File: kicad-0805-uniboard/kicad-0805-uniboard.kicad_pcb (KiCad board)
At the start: 2 copper layers, 100 x 110 mm, 140 parts, among them J1 ICSP Header, J102 Conn_01x16_Male, J103 BA56_3DIG_7SEG, J104 Gate Out, J105 Clock Out, J106 Clock In, J107 Pitch Out, J108 CV Out, J109 Reset In, J4 RED_STRIPE, Q1 2N7002, Q101 MMBT3906, Q102 MMBT3906, Q103 MMBT3906, Q104 MMBT3904, Q105 MMBT3904, Q2 2N7002, Q3 2N7002, Q4 2N7002, SW101 Shift, SW102 Play, SW103 Load, SW104 Save, SW105 Repeat, SW106 Mutate, SW107 Glide, SW108 SW_Push, SW109 SW_Push, SW110 SW_Push, SW111 SW_Push, SW112 SW_Push, SW113 SW_Push, SW114 SW_Push, SW115 SW_Push, SW116 Rotary_Encoder, SW117 SW_Push, SW118 SW_Push, SW119 SW_Push, SW120 SW_Push, SW121 SW_Push, SW122 SW_Push, SW123 SW_Push, SW124 SW_Push, U1 AMS1117-5.0, U101 74HC595, U102 MCP23S17, U103 74HC595, U2 AMS1117-3.3, U3 ATMega328P, U4 W25Q80DVSN, U5 TL072, U6 MCP4822, Y1 16 MHz

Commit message: Initial fp's changed. Cleared old routings.
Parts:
- removed J102: Conn_01x16_Male, Pin_Headers:Pin_Header_Straight_1x16_Pitch2.54mm
- added C10: 10uF, Capacitor_SMD:CP_Elec_5x5.7, F.Cu at (220.7, 129.7)
- added C11: 100uF, Capacitor_SMD:CP_Elec_6.3x7.7, F.Cu at (211.0, 130.3)
- added C12: 22uF, Capacitor_SMD:CP_Elec_5x5.7, F.Cu at (219.2, 137.8)
- added C2: 22uF, Capacitor_SMD:CP_Elec_5x5.7, F.Cu at (210.2, 137.8)
- C104, C107: footprint Capacitors_SMD:CP_Elec_6.3x7.7 -> Capacitor_SMD:CP_Elec_5x5.7
- C16: footprint Capacitor_SMD:C_0805_2012Metric_Pad1.15x1.40mm_HandSolder -> Capacitor_SMD:CP_Elec_5x5.7
- RV101, RV102, RV103, RV104: footprint Potentiometers:Potentiometer_Alps_RK09K_Horizontal -> Eurocad:Alpha9mmPot-SemiSMD4
- moved D109 52.6 mm to (130.1, 127.8)
- moved C1 52.6 mm to (240.0, 87.0)
- moved C101 52.6 mm to (131.1, 114.2)
- moved C102 52.6 mm to (126.1, 114.2)
- moved C103 52.6 mm to (123.1, 114.2)
- moved C105 52.6 mm to (66.1, 115.2)
- moved C106 52.6 mm to (68.1, 115.2)
- moved C107 52.6 mm to (148.1, 65.2)
- moved C108 52.6 mm to (139.4, 60.9)
- moved C109 52.6 mm to (139.4, 58.2)
- moved C14 52.6 mm to (215.2, 109.7)
- moved C15 52.6 mm to (226.5, 98.8)
- moved C4 52.6 mm to (241.5, 90.0)
- moved C7 52.6 mm to (210.5, 109.7)
- moved C8 52.6 mm to (240.0, 84.1)
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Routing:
- net +5V: track 413.6 -> 0.00 mm, vias 2 -> 0
- net Net-(SW109-Pad2): track 218.8 -> 0.00 mm
- net Net-(SW108-Pad2): track 146.6 -> 0.00 mm
- net /A3: track 139.7 -> 0.00 mm
- net Net-(D101-Pad1): track 136.6 -> 0.00 mm
- net /A2: track 123.3 -> 0.00 mm
- net ResetIn: track 116.1 -> 0.00 mm
- net Net-(D102-Pad1): track 108.2 -> 0.00 mm
- net Net-(SW112-Pad1): track 107.8 -> 0.00 mm
- net Net-(U101-Pad9): track 100.8 -> 0.00 mm, vias 2 -> 0
- net GND: track 95.8 -> 0.00 mm, vias 14 -> 1
- net Net-(SW117-Pad1): track 94.7 -> 0.00 mm
- net /A1: track 94.4 -> 0.00 mm
- net AD1: track 91.7 -> 0.00 mm
- net Net-(D103-Pad1): track 78.9 -> 0.00 mm
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- added copper zone on F.Cu, net GND
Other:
- outline, holes or cut-outs redrawn

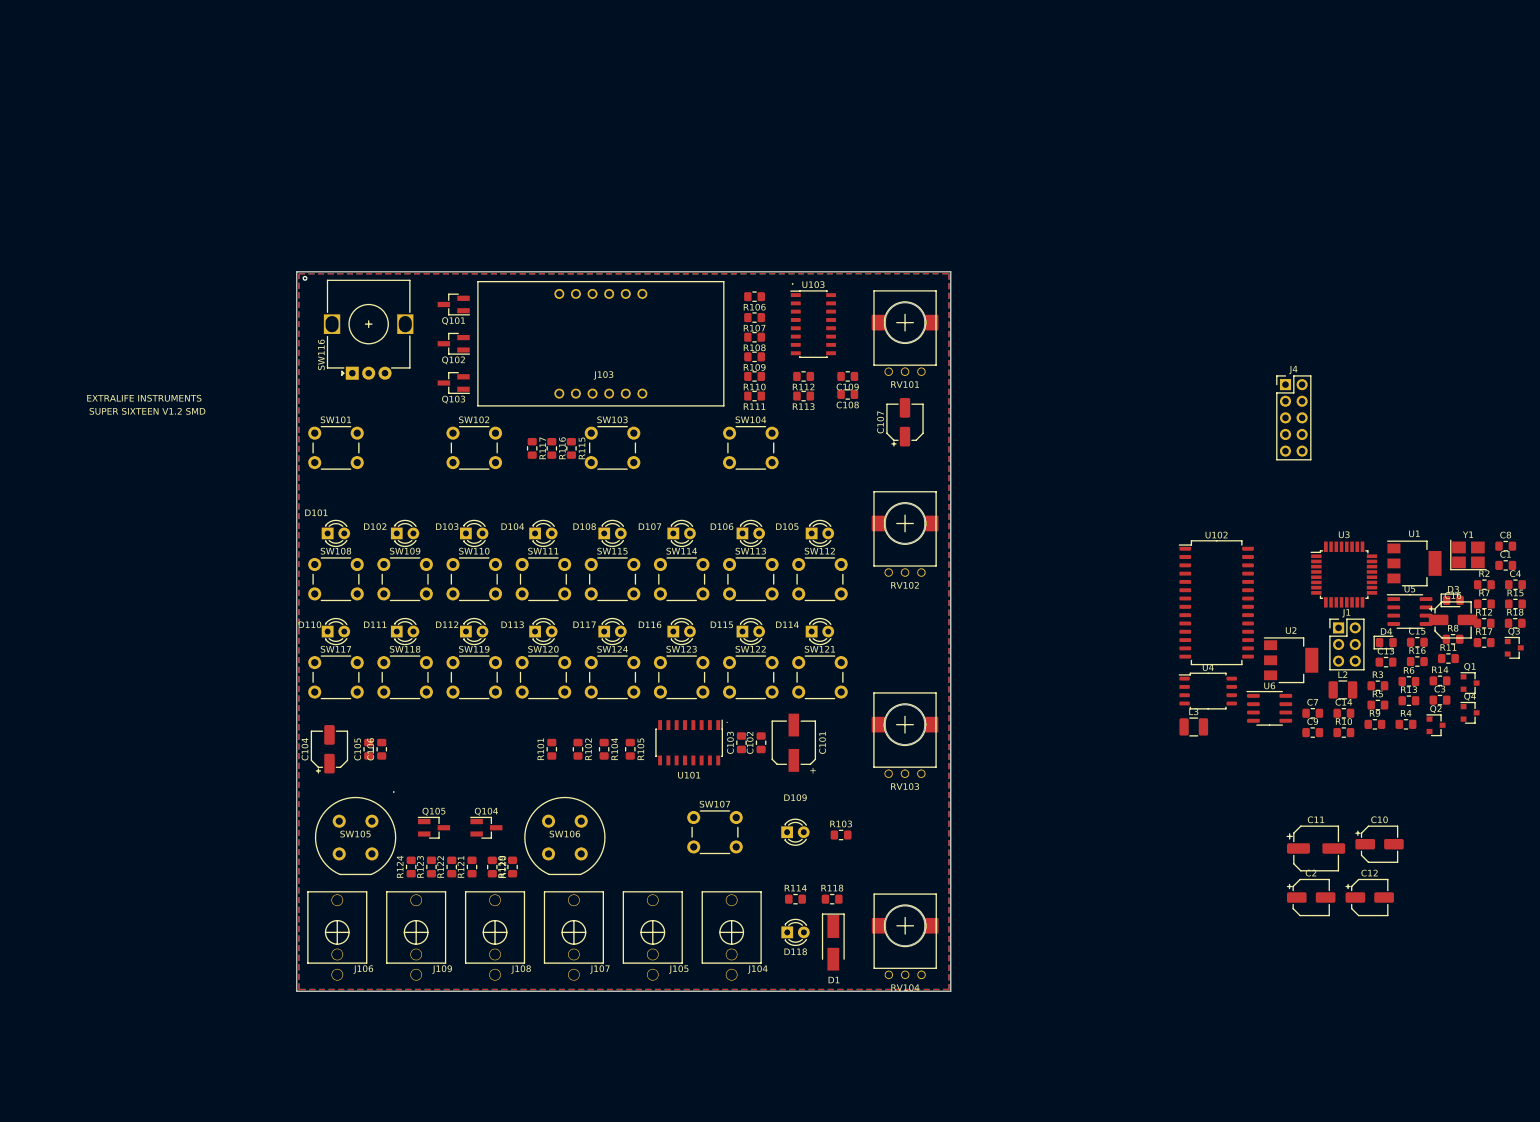
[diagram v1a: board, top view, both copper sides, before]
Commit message: Forgot some schematic stuff. More placement.
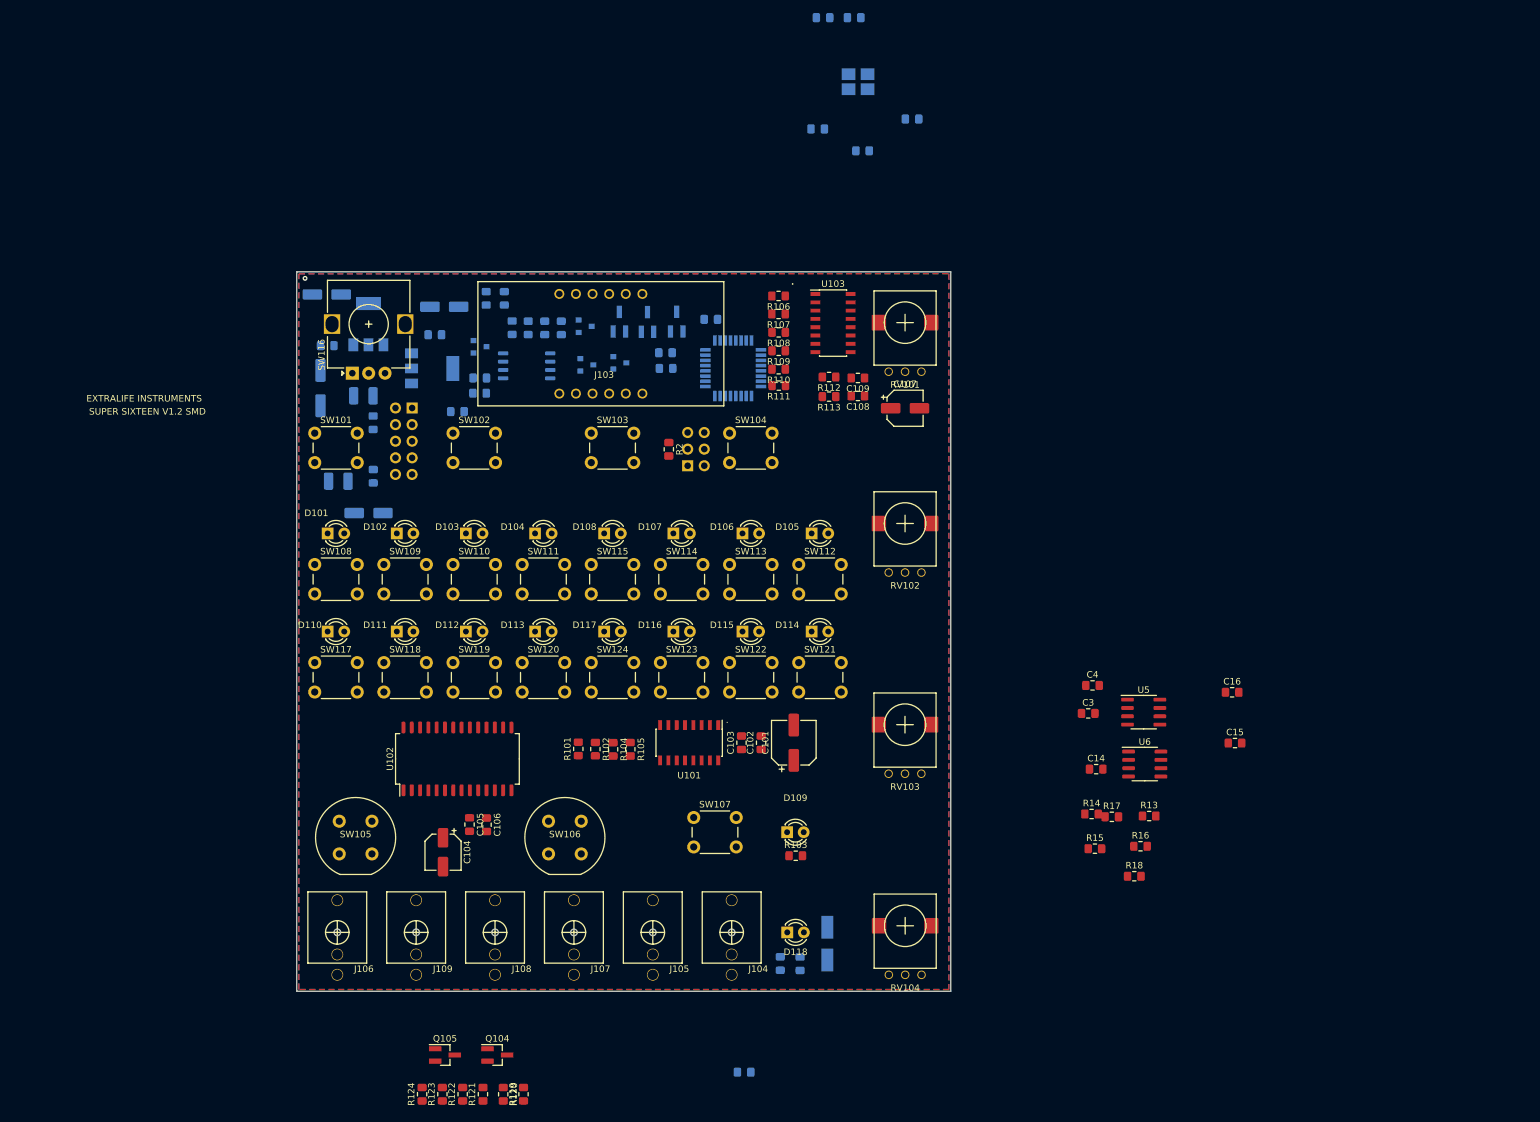
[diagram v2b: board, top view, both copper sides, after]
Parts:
- added C5: 100nF, Capacitor_SMD:C_0805_2012Metric_Pad1.15x1.40mm_HandSolder, B.Cu at (135.6, 3.30)
- added C6: 100nF, Capacitor_SMD:C_0805_2012Metric_Pad1.15x1.40mm_HandSolder, B.Cu at (140.3, 3.30)
- C1, C10, C11, C12, C13, C2, C7, C8, C9, D1, D3, D4, J1, J4, L2, L3, Q1, Q101, Q102, Q103, Q2, Q3, Q4, R10, R11, R114, R115, R116, R117, R118, R12, R3, R4, R5, R6, R7, R8, R9, U1, U2, U3, U4, Y1: moved to B.Cu
- C101: footprint Capacitors_SMD:CP_Elec_6.3x7.7 -> Capacitor_SMD:CP_Elec_6.3x7.7
- C16: footprint Capacitor_SMD:CP_Elec_5x5.7 -> Capacitor_SMD:C_0805_2012Metric_Pad1.15x1.40mm_HandSolder
- moved C1 183.3 mm to (59.8, 53.5)
- moved C2 176.5 mm to (59.7, 45.6)
- moved C11 167.7 mm to (58.8, 59.9), turned to 90 degrees
- moved D3 167.4 mm to (66.8, 65.2), turned to 270 degrees
- moved C10 164.9 mm to (77.7, 47.5), turned to 180 degrees
- moved U1 164.1 mm to (66.1, 50.2), turned to 90 degrees
- moved C12 164.0 mm to (66.1, 79.0), turned to 180 degrees
- moved R7 159.8 mm to (79.7, 63.5), turned to 180 degrees
- moved Q2 157.2 mm to (83.1, 53.6)
- moved D4 157.0 mm to (66.8, 73.4), turned to 270 degrees
- moved L2 156.4 mm to (65.3, 61.1)
- moved R11 153.6 mm to (83.1, 60.7), turned to 180 degrees
- moved R12 153.0 mm to (90.5, 50.7), turned to 270 degrees
- moved C13 148.4 mm to (84.1, 46.2), turned to 270 degrees
- moved Q3 148.2 mm to (99.5, 56.4)
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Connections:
- C11 pad 1: Net-(C11-Pad1) -> +12V
- C12 pad 2: Net-(C12-Pad2) -> -12V
- D3 pad 1: +12V -> Net-(D3-Pad1)
- D4 pad 2: -12V -> Net-(D4-Pad2)
- L2 pad 1: Net-(C11-Pad1) -> +12V
- L2 pad 2: +12V -> Net-(D3-Pad1)
- L3 pad 1: Net-(C12-Pad2) -> -12V
- L3 pad 2: -12V -> Net-(D4-Pad2)
- U3 pad 18: Net-(U3-Pad18) -> +5V
- U3 pad 20: Net-(U3-Pad20) -> +5V
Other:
- outline, holes or cut-outs redrawn

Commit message: More placement work.
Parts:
- C14, C15, C16, C3, C4, Q104, R119, R120, R121, R13, R14, R15, R16, R17, R18, U5, U6: moved to B.Cu
- R4: moved to F.Cu
- moved R119 63.8 mm to (63.9, 109.6), turned to 0 degrees
- moved R122 60.6 mm to (63.9, 109.6), turned to 0 degrees
- moved R120 52.9 mm to (66.2, 119.1)
- moved R121 52.7 mm to (63.6, 119.1), turned to 270 degrees
- moved Q104 52.3 mm to (64.9, 113.9), turned to 270 degrees
- moved R123 50.0 mm to (66.2, 119.1), turned to 270 degrees
- moved R124 49.9 mm to (63.6, 119.1), turned to 270 degrees
- moved Q105 49.7 mm to (64.9, 113.9), turned to 270 degrees
- moved C15 36.4 mm to (162.2, 116.0), turned to 180 degrees
- moved C16 35.6 mm to (162.6, 108.2), turned to 180 degrees
- moved R4 31.9 mm to (110.6, 135.4), turned to 180 degrees
- moved R13 10.3 mm to (175.3, 127.1), turned to 180 degrees
- moved U6 8.98 mm to (176.0, 119.2), turned to 180 degrees
- moved C3 8.66 mm to (184.6, 111.4), turned to 180 degrees
- moved U5 8.66 mm to (176.1, 111.2), turned to 180 degrees
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
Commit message: Prepped to throw more stuff on there..
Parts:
- moved C2 0.35 mm to (59.4, 45.5)
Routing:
- net +5V: track 0.00 -> 89.9 mm
- net +12V: track 0.00 -> 29.7 mm
- net Net-(D3-Pad2): track 0.00 -> 8.33 mm
- net Net-(D3-Pad1): track 0.00 -> 3.09 mm
- net GND: vias 1 -> 0
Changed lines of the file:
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@@
     (thickness 1.6)
     (drawings 16)
-    (tracks 1)
+    (tracks 24)
     (zones 0)
     (modules 145)
@@
   (page A4)
   (layers
-    (0 F.Cu signal)
+    (0 F.Cu signal hide)
     (31 B.Cu signal)
     (32 B.Adhes user)
-    (33 F.Adhes user)
+    (33 F.Adhes user hide)
     (34 B.Paste user)
-    (35 F.Paste user)
+    (35 F.Paste user hide)
     (36 B.SilkS user)
-    (37 F.SilkS user)
+    (37 F.SilkS user hide)
     (38 B.Mask user)
-    (39 F.Mask user)
-    (40 Dwgs.User user)
+    (39 F.Mask user hide)
+    (40 Dwgs.User user hide)
     (41 Cmts.User user)
     (42 Eco1.User user)
@@
     (45 Margin user)
     (46 B.CrtYd user)
-    (47 F.CrtYd user)
+    (47 F.CrtYd user hide)
     (48 B.Fab user)
-    (49 F.Fab user)
+    (49 F.Fab user hide)
   )
   (setup
-    (last_trace_width 0.25)
+    (last_trace_width 0.4)
     (user_trace_width 0.3)
     (user_trace_width 0.35)
@@
   )
   (module Capacitor_SMD:CP_Elec_5x5.7 (layer B.Cu)
-    (at 59.71 45.62)
+    (at 59.39 45.49)
     (descr "SMD capacitor, aluminum electrolytic, United Chemi-Con, 5.0x5.7mm")
     (tags "capacitor electrolytic")
@@
   (gr_line (start 55.12 152.16) (end 155.12 152.16) (layer Edge.Cuts) (width 0.05))
   (gr_line (start 55.12 42.16) (end 55.12 152.16) (layer Edge.Cuts) (width 0.05))
-  (via (at 56.39 43.16) (size 0.75) (drill 0.35) (layers F.Cu B.Cu) (net 1))
+  (segment (start 66.08 51.91) (end 66.08 47.01) (width 0.4) (layer B.Cu) (net 2))
+  (segment (start 66.08 53.31) (end 66.08 51.91) (width 0.4) (layer B.Cu) (net 2))
+  (segment (start 57.51 44.82) (end 59.55 42.78) (width 0.4) (layer B.Cu) (net 2))
+  (segment (start 57.51 45.62) (end 57.51 44.82) (width 0.4) (layer B.Cu) (net 2))
+  (segment (start 59.55 42.78) (end 139.43 42.78) (width 0.4) (layer B.Cu) (net 2))
+  (segment (start 62.305 62.64) (end 63.825 61.12) (width 0.4) (layer B.Cu) (net 83))
+  (segment (start 58.75 62.64) (end 62.305 62.64) (width 0.4) (layer B.Cu) (net 83))
+  (segment (start 60.81 60.58) (end 60.81 53.45) (width 0.4) (layer B.Cu) (net 83))
+  (segment (start 58.75 62.64) (end 60.81 60.58) (width 0.4) (layer B.Cu) (net 83))
+  (segment (start 63.64 53.45) (end 63.78 53.31) (width 0.4) (layer B.Cu) (net 83))
+  (segment (start 60.81 53.45) (end 63.64 53.45) (width 0.4) (layer B.Cu) (net 83))
+  (segment (start 63.78 54.71) (end 64.47 55.4) (width 0.4) (layer B.Cu) (net 83))
+  (segment (start 63.78 53.31) (end 63.78 54.71) (width 0.4) (layer B.Cu) (net 83))
+  (segment (start 64.47 55.4) (end 70.46 55.4) (width 0.4) (layer B.Cu) (net 83))
+  (segment (start 71.23 54.63) (end 72.67 54.63) (width 0.4) (layer B.Cu) (net 83))
+  (segment (start 70.46 55.4) (end 71.23 54.63) (width 0.4) (layer B.Cu) (net 83))
+  (segment (start 72.76 62.98) (end 70.22 62.98) (width 0.4) (layer B.Cu) (net 92))
+  (segment (start 67.5 66.26) (end 68.47 65.29) (width 0.4) (layer B.Cu) (net 92))
+  (segment (start 66.8 66.26) (end 67.5 66.26) (width 0.4) (layer B.Cu) (net 92))
+  (segment (start 68.47 65.29) (end 68.47 63.56) (width 0.4) (layer B.Cu) (net 92))
+  (segment (start 68.47 63.56) (end 69.03 63) (width 0.4) (layer B.Cu) (net 92))
+  (segment (start 70.2 63) (end 70.22 62.98) (width 0.4) (layer B.Cu) (net 92))
+  (segment (start 69.03 63) (end 70.2 63) (width 0.4) (layer B.Cu) (net 92))
+  (segment (start 66.8 64.21) (end 66.8 61.12) (width 0.4) (layer B.Cu) (net 117))
   (zone (net 1) (net_name GND) (layer F.Cu) (hatch edge 0.508)
     (connect_pads (clearance 0.35))

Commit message: Initial placement complete.
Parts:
- C14, C15, R13, R15, R17, U6: moved to F.Cu
- moved R3 117.2 mm to (132.7, 137.5), turned to 270 degrees
- moved C14 111.6 mm to (86.9, 64.0), turned to 0 degrees
- moved C3 105.6 mm to (85.9, 74.1), turned to 0 degrees
- moved U6 98.4 mm to (93.2, 65.9), turned to 0 degrees
- moved R16 93.6 mm to (83.0, 133.1), turned to 270 degrees
- moved U5 90.3 mm to (93.1, 75.8)
- moved R18 89.5 mm to (88.1, 133.1), turned to 270 degrees
- moved C4 88.4 mm to (100.6, 77.8), turned to 0 degrees
- moved C16 81.0 mm to (85.6, 133.1), turned to 90 degrees
- moved R15 77.1 mm to (106.5, 131.9), turned to 90 degrees
- moved R13 71.5 mm to (104.0, 131.8), turned to 270 degrees
- moved C5 66.5 mm to (118.5, 67.6), turned to 90 degrees
- moved R14 65.1 mm to (119.0, 127.9)
- moved C8 61.5 mm to (107.3, 63.8), turned to 180 degrees
- moved Y1 56.8 mm to (112.7, 62.4)
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
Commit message: More routes.
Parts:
- R14: moved to F.Cu
- R17: moved to B.Cu
- moved R17 62.4 mm to (90.2, 132.9), turned to 90 degrees
- moved R14 8.70 mm to (110.4, 126.3), turned to 270 degrees
- moved R7 3.44 mm to (83.1, 63.1), turned to 0 degrees
- moved R18 0.85 mm to (87.3, 132.9)
- moved R16 0.85 mm to (82.2, 132.9)
- moved C16 0.85 mm to (84.8, 132.9)
- turned R11 to 0 degrees
- turned R5 to 0 degrees
- turned R9 to 270 degrees
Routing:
- net +5V: track 89.9 -> 371.2 mm, vias 0 -> 1
- net +3V3: track 0.00 -> 44.1 mm
- net -12V: track 0.00 -> 7.82 mm
- net Net-(D4-Pad1): track 0.00 -> 6.25 mm
- net +12V: track 29.7 -> 34.4 mm
- net Net-(D4-Pad2): track 0.00 -> 3.97 mm
- net GND: vias 0 -> 1

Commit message: More routing. This will be tightgit status .
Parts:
- moved J1 25.0 mm to (136.6, 74.8)
- moved R2 25.0 mm to (133.8, 72.3)
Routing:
- net ENC1: track 0.00 -> 91.0 mm, vias 0 -> 1
- net ENC2: track 0.00 -> 85.2 mm, vias 0 -> 1
- net +5V: track 371.2 -> 435.7 mm, vias 1 -> 3
- net +12V: track 34.4 -> 80.5 mm, vias 0 -> 2
- net Net-(Q2-Pad2): track 0.00 -> 21.5 mm
- net Net-(R111-Pad1): track 0.00 -> 11.7 mm
- net Net-(R106-Pad1): track 0.00 -> 11.6 mm
- net Net-(R113-Pad1): track 0.00 -> 10.3 mm
- net Net-(R110-Pad1): track 0.00 -> 10.3 mm
- net Net-(R109-Pad1): track 0.00 -> 8.65 mm
- net Net-(R112-Pad1): track 0.00 -> 8.24 mm
- net Net-(R108-Pad1): track 0.00 -> 7.71 mm
- net Net-(R107-Pad1): track 0.00 -> 6.99 mm
- net CS2: track 0.00 -> 6.79 mm, vias 0 -> 1
- net -12V: track 7.82 -> 11.8 mm
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
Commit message: It won't work this way!
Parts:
- C108, C109, R112, R113, U103: moved to B.Cu
- C7, C8: moved to F.Cu
- Y1: value 16 MHz -> 16MHz; footprint Crystal:Crystal_SMD_3225-4Pin_3.2x2.5mm_HandSoldering -> Crystal:Crystal_HC49-4H_Vertical
- moved R112 40.7 mm to (177.2, 59.9), turned to 0 degrees
- moved R113 40.7 mm to (177.2, 62.9), turned to 0 degrees
- moved U103 30.8 mm to (167.9, 49.3), turned to 180 degrees
- moved C108 24.6 mm to (165.5, 62.8), turned to 0 degrees
- moved C109 24.6 mm to (165.5, 60.1), turned to 0 degrees
- moved C5 5.70 mm to (123.7, 65.1)
- moved C7 5.22 mm to (116.9, 68.8)
- moved C14 3.77 mm to (88.9, 67.2), turned to 90 degrees
- moved C6 2.87 mm to (121.5, 48.8), turned to 270 degrees
- moved C8 2.60 mm to (109.9, 63.9)
- moved R115 1.59 mm to (117.7, 49.0), turned to 90 degrees
- moved U6 1.56 mm to (93.5, 67.5), turned to 90 degrees
- moved Y1 1.53 mm to (113.2, 63.9), turned to 270 degrees
- moved R8 1.27 mm to (95.8, 49.5), turned to 90 degrees
- moved R116 0.94 mm to (110.6, 56.8)
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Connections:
- Y1 pad 2: GND -> Net-(C7-Pad2)
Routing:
- net SCK: track 0.00 -> 67.1 mm, vias 0 -> 6
- net MOSI: track 0.00 -> 57.2 mm, vias 0 -> 4
- net +5V: track 435.7 -> 478.5 mm, vias 3 -> 4
- net Net-(Q4-Pad2): track 0.00 -> 42.1 mm, vias 0 -> 2
- net Net-(J103-Pad11): track 0.00 -> 36.0 mm
- net -12V: track 11.8 -> 47.0 mm
- net CS2: track 6.79 -> 41.5 mm, vias 1 -> 3
- net Net-(Q1-Pad2): track 0.00 -> 29.3 mm, vias 0 -> 2
- net Net-(J103-Pad10): track 0.00 -> 28.2 mm, vias 0 -> 1
- net MISO: track 0.00 -> 27.7 mm, vias 0 -> 2
- net +3V3: track 44.1 -> 71.0 mm
- net Net-(J103-Pad7): track 0.00 -> 23.5 mm
- net Net-(U5-Pad3): track 0.00 -> 20.7 mm, vias 0 -> 1
- net Net-(J103-Pad12): track 0.00 -> 20.5 mm, vias 0 -> 1
- net Net-(Q3-Pad2): track 0.00 -> 20.2 mm, vias 0 -> 2
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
